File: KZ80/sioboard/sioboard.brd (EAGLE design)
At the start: 100 x 80 mm, 18 parts, among them J1 CLKSEL

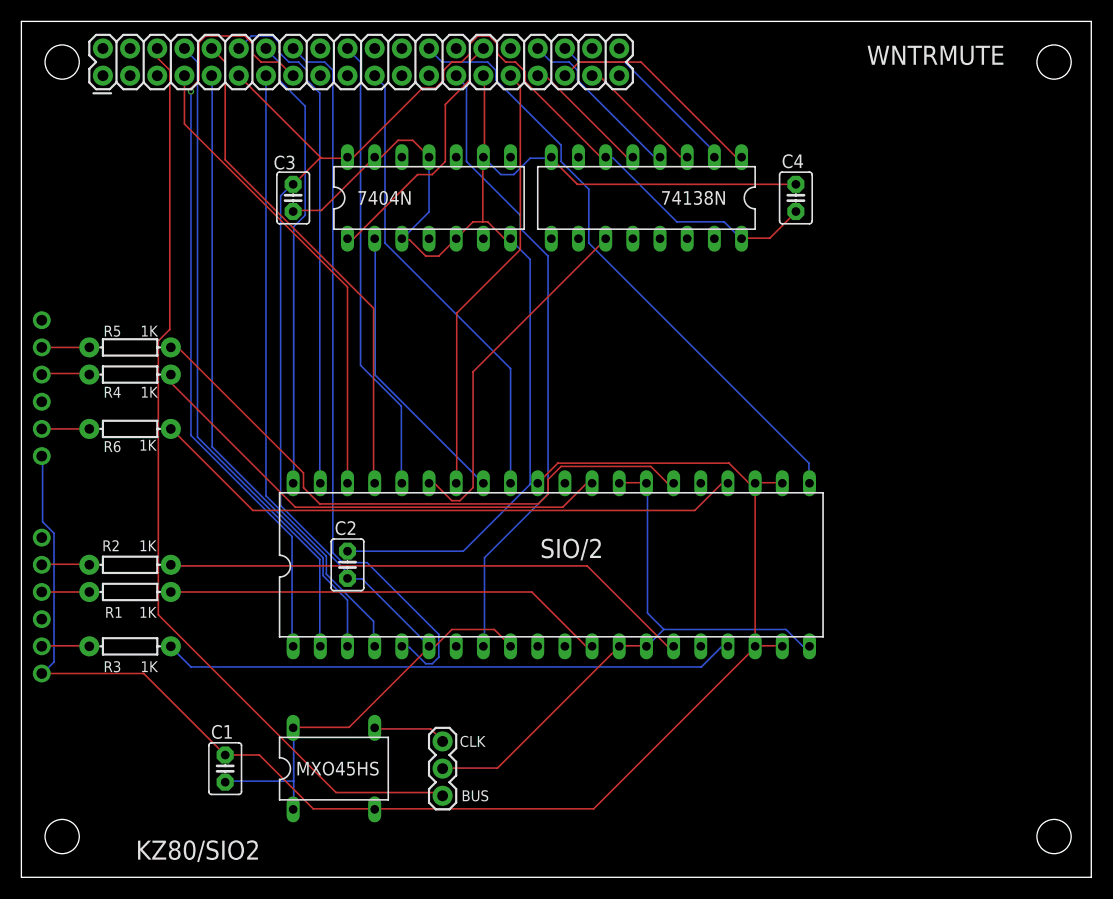
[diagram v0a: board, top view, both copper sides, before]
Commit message: sioboard: adjust layout and add ground plane.
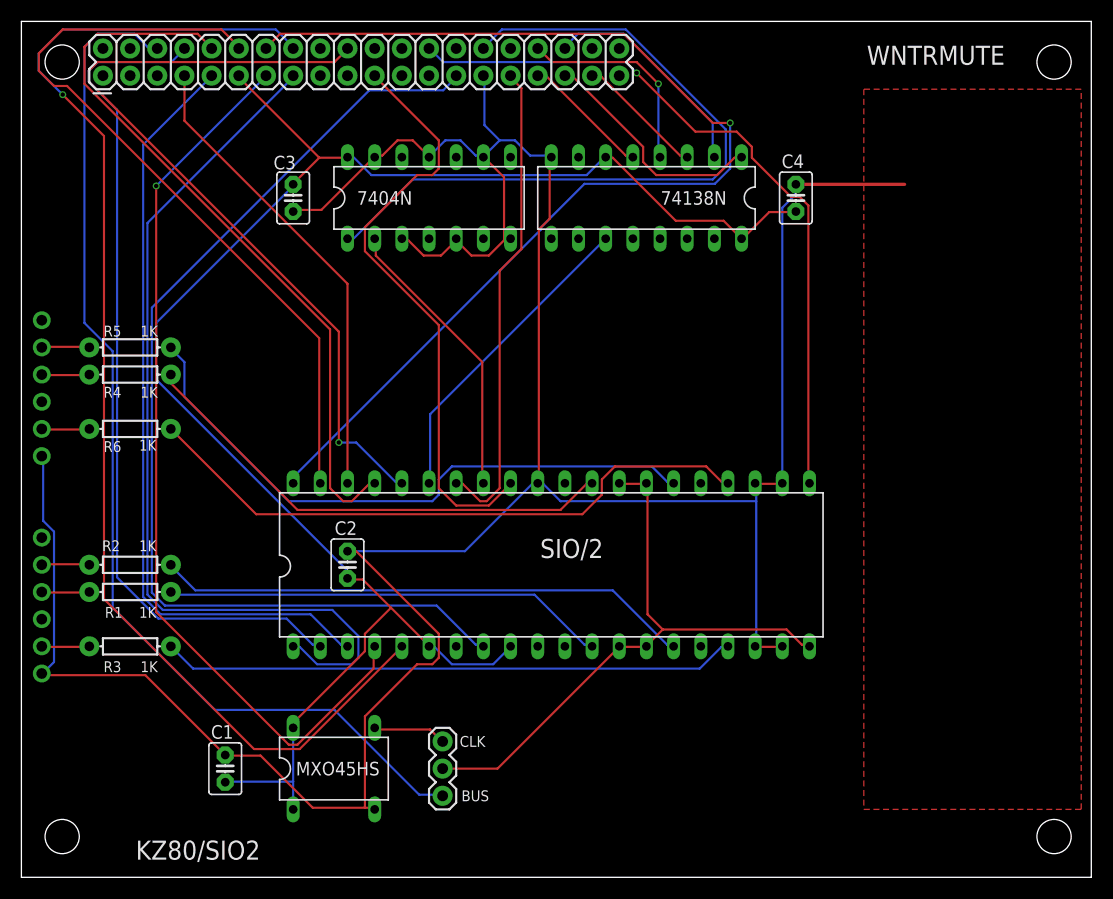
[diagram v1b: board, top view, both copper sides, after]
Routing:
- net D0: track 42.6 -> 105.2 mm, vias 0 -> 1
- net INT: track 69.2 -> 116.7 mm, vias 0 -> 1
- net N$11: track 24.2 -> 68.9 mm
- net M1: track 59.4 -> 97.2 mm
- net IORQ: track 42.7 -> 77.1 mm, vias 0 -> 1
- net D7: track 57.6 -> 84.9 mm, vias 0 -> 1
- net D2: track 47.8 -> 72.2 mm
- net D6: track 47.0 -> 69.1 mm
- net D3: track 61.1 -> 80.0 mm
- net D5: track 58.6 -> 72.5 mm
- net D1: track 71.8 -> 84.6 mm, vias 1 -> 0
- net RD: track 43.4 -> 55.9 mm
- net N$3: track 87.5 -> 99.5 mm
- net GND: track 269.2 -> 279.6 mm
- net RESET: track 57.9 -> 68.1 mm, vias 0 -> 1
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- added copper zone on layer 1, net GND

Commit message: sioboard: break out interrupt priority pins.
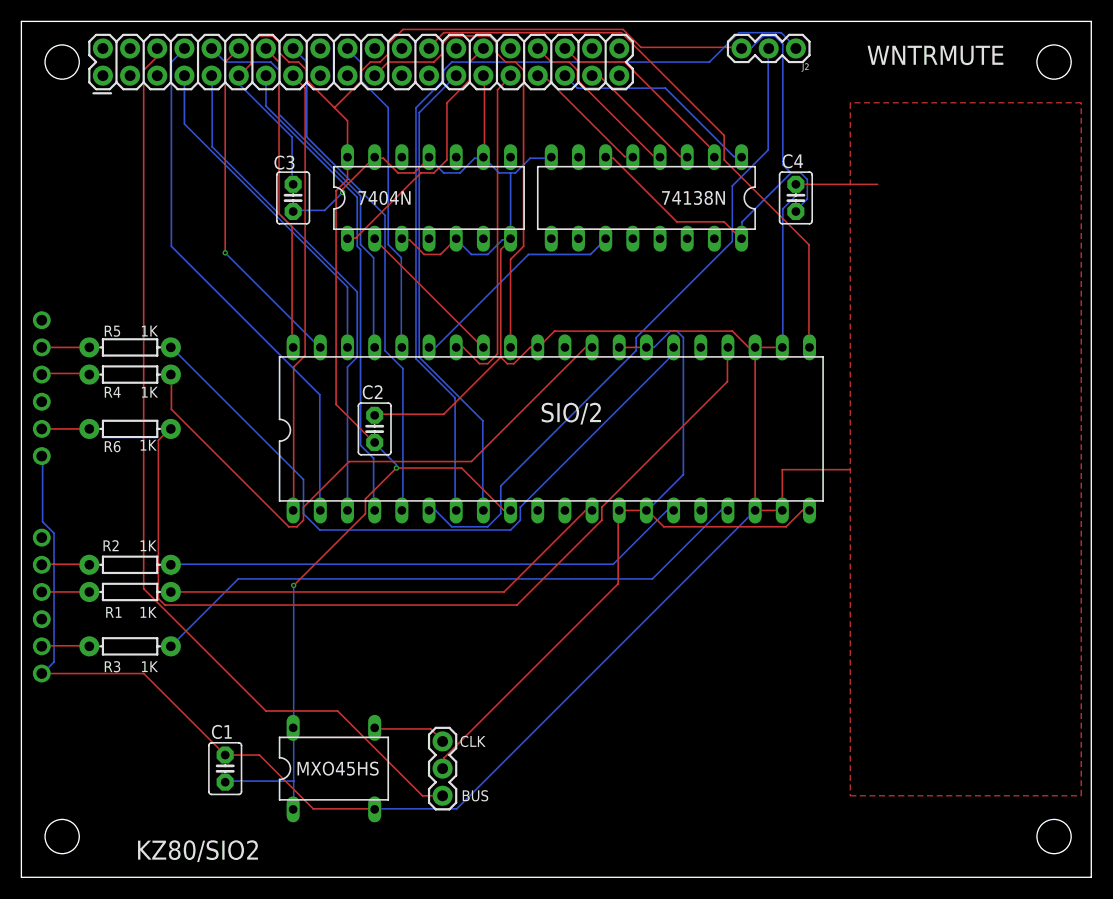
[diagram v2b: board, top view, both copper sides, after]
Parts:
- added J2: IESEL, SparkFun-Connectors:1X03
- moved C2 13.0 mm to (33.0, 41.9)
- moved U$2 12.7 mm to (49.5, 41.9)
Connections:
- new net N$25: J2.1, U$2.7
- new net N$26: J2.2, U$2.6
- net VCC: now also J2.3; no longer U$2.6
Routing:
- net N$25: track 0.00 -> 78.9 mm
- net D0: track 105.2 -> 29.1 mm, vias 1 -> 0
- net INT: track 116.7 -> 47.5 mm, vias 1 -> 0
- net N$26: track 0.00 -> 61.7 mm
- net M1: track 97.2 -> 44.6 mm
- net IORQ: track 77.1 -> 30.1 mm, vias 1 -> 0
- net VCC: track 162.4 -> 208.5 mm, vias 0 -> 2
- net N$11: track 68.9 -> 24.2 mm
- net D1: track 84.6 -> 41.6 mm
- net D2: track 72.2 -> 32.2 mm, vias 0 -> 1
- net D7: track 84.9 -> 44.9 mm, vias 1 -> 0
- net D6: track 69.1 -> 36.8 mm
- net D3: track 80.0 -> 49.5 mm
- net D5: track 72.5 -> 46.6 mm
- net N$23: track 58.8 -> 82.4 mm
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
